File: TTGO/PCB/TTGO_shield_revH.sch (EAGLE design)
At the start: 43 parts

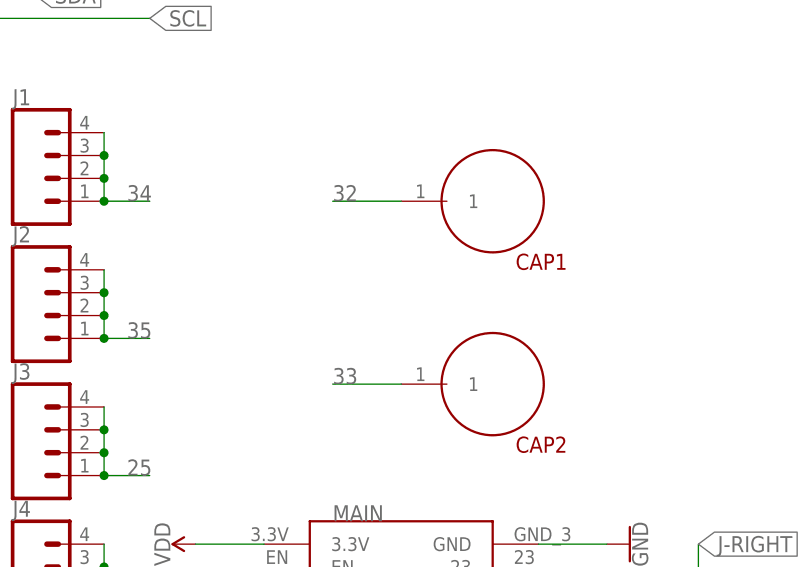
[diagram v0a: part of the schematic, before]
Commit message: updated capsense buttons to clear oshpark drc
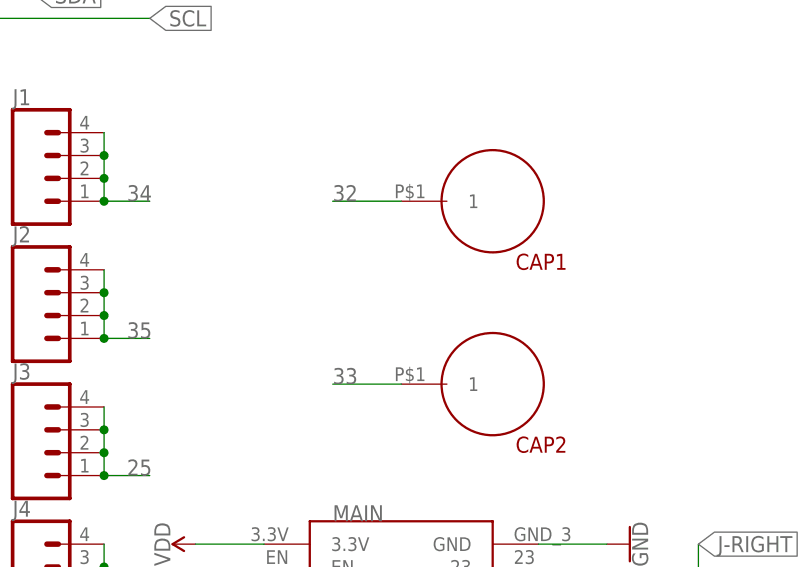
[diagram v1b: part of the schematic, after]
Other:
- moved on the sheet: CAP1, CAP2
